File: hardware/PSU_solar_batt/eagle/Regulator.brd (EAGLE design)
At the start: 60.3 x 63.2 mm, 28 parts, among them IC1 MCP3550-60MS, IC2 MCP3550-60MS, IC3 MCP73831/OT

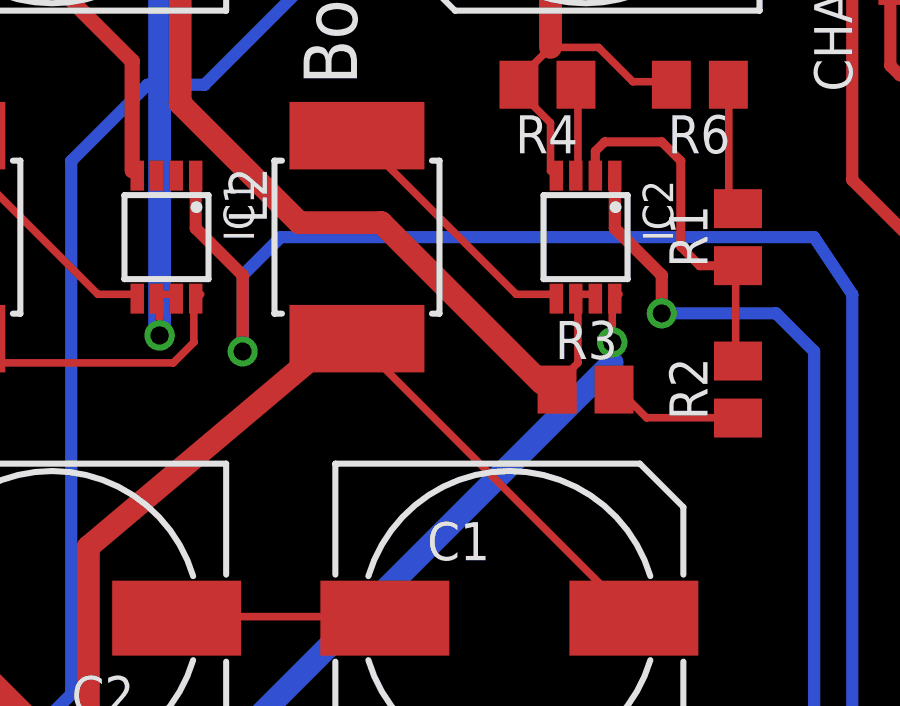
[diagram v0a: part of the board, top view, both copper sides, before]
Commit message: renames IC1 and IC2 to MCP1642 to avoid confusion (currently MCP3550 part is used instead because MCP1642 is not in the Microchip library)
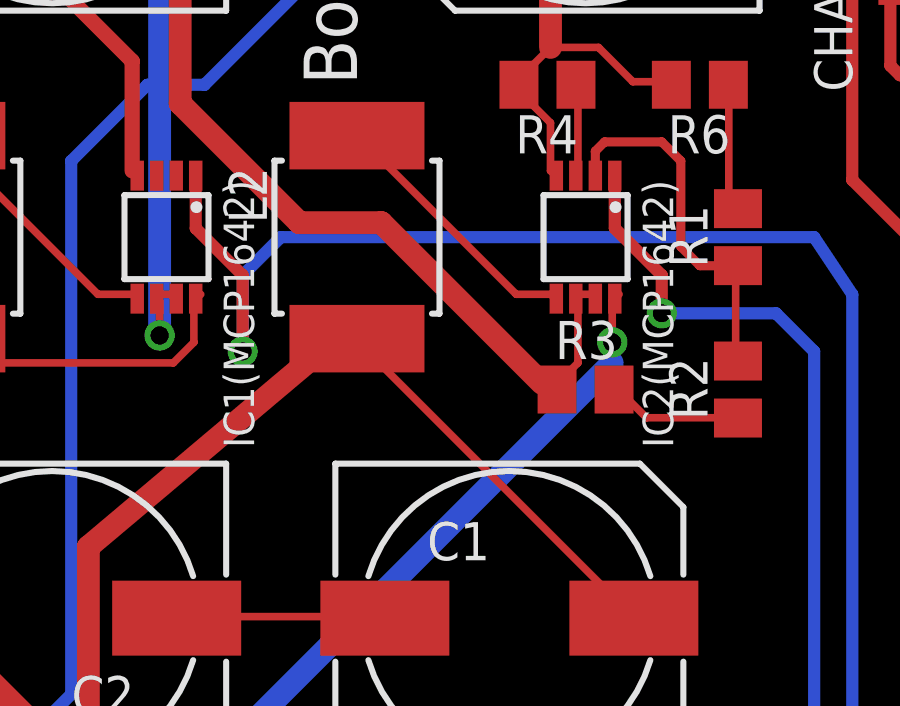
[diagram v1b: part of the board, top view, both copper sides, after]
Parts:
- renumbered IC1 to IC1(MCP1642), IC2 to IC2(MCP1642)
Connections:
- net N$1 renamed MCP1642
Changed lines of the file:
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@@
 <?xml version="1.0" encoding="utf-8"?>
 <!DOCTYPE eagle SYSTEM "eagle.dtd">
-<eagle version="7.2.0">
+<eagle version="7.1.0">
 <drawing>
 <settings>
@@
 <element name="C3" library="rcl" package="140CLH-1010" value="10uF" x="7.62" y="43.18" rot="R180"/>
 <element name="C4" library="rcl" package="140CLH-1010" value="10uF" x="25.4" y="43.18" rot="R180"/>
-<element name="IC1" library="microchip" package="MSOP8" value="MCP3550-60MS" x="11.43" y="30.48" smashed="yes" rot="R180">
+<element name="IC1(MCP1642)" library="microchip" package="MSOP8" value="MCP3550-60MS" x="11.43" y="30.48" smashed="yes" rot="R180">
 <attribute name="OC_NEWARK" value="69K0134" x="11.43" y="30.48" size="1.778" layer="27" rot="R180" display="off"/>
 <attribute name="MPN" value="MCP3550-60E/MS" x="11.43" y="30.48" size="1.778" layer="27" rot="R180" display="off"/>
@@
 <attribute name="NAME" x="13.335" y="32.385" size="1.016" layer="25" rot="R270"/>
 </element>
-<element name="IC2" library="microchip" package="MSOP8" value="MCP3550-60MS" x="25.4" y="30.48" smashed="yes" rot="R180">
+<element name="IC2(MCP1642)" library="microchip" package="MSOP8" value="MCP3550-60MS" x="25.4" y="30.48" smashed="yes" rot="R180">
 <attribute name="OC_NEWARK" value="69K0134" x="25.4" y="30.48" size="1.778" layer="27" rot="R180" display="off"/>
 <attribute name="MPN" value="MCP3550-60E/MS" x="25.4" y="30.48" size="1.778" layer="27" rot="R180" display="off"/>
@@
 </elements>
 <signals>
-<signal name="N$1">
+<signal name="MCP1642">
 <contactref element="C2" pad="+"/>
 <contactref element="L1" pad="2"/>
 <contactref element="REGULATORS" pad="4"/>
-<contactref element="IC1" pad="8"/>
+<contactref element="IC1(MCP1642)" pad="8"/>
 <wire x1="7.5438" y1="13.716" x2="7.5438" y2="10.287" width="0.762" layer="1"/>
 <wire x1="3.6576" y1="17.6022" x2="7.5438" y2="13.716" width="0.762" layer="1"/>
@@
 <contactref element="C1" pad="+"/>
 <contactref element="L2" pad="2"/>
-<contactref element="IC2" pad="8"/>
+<contactref element="IC2(MCP1642)" pad="8"/>
 <wire x1="17.8308" y1="26.9748" x2="26.9748" y2="17.8308" width="0.254" layer="1"/>
 <wire x1="26.9748" y1="17.8308" x2="27.01" y2="17.78" width="0.254" layer="1"/>
@@
 </signal>
 <signal name="3.3V">
-<contactref element="IC1" pad="4"/>
+<contactref element="IC1(MCP1642)" pad="4"/>
 <contactref element="C3" pad="+"/>
 <contactref element="3.3VOUT" pad="2"/>
@@
 <signal name="N$2">
 <contactref element="L1" pad="1"/>
-<contactref element="IC1" pad="5"/>
+<contactref element="IC1(MCP1642)" pad="5"/>
 <wire x1="9.144" y1="28.575" x2="10.287" y2="28.575" width="0.254" layer="1"/>
 <wire x1="3.8862" y1="33.8328" x2="9.144" y2="28.575" width="0.254" layer="1"/>
@@
 <signal name="N$4">
 <contactref element="L2" pad="1"/>
-<contactref element="IC2" pad="5"/>
+<contactref element="IC2(MCP1642)" pad="5"/>
 <wire x1="23.0886" y1="28.575" x2="24.2316" y2="28.575" width="0.254" layer="1"/>
 <wire x1="17.8308" y1="33.8328" x2="23.0886" y2="28.575" width="0.254" layer="1"/>
@@
 </signal>
 <signal name="5V">
-<contactref element="IC2" pad="4"/>
+<contactref element="IC2(MCP1642)" pad="4"/>
 <contactref element="R4" pad="2"/>
 <contactref element="C4" pad="+"/>
@@
 </signal>
 <signal name="N$10">
-<contactref element="IC2" pad="2"/>
+<contactref element="IC2(MCP1642)" pad="2"/>
 <contactref element="R2" pad="2"/>
 <contactref element="R1" pad="1"/>
@@
 </signal>
 <signal name="CONN">
-<contactref element="IC2" pad="3"/>
+<contactref element="IC2(MCP1642)" pad="3"/>
 <contactref element="R4" pad="1"/>
 <wire x1="25.146" y1="35.433" x2="25.146" y2="32.6898" width="0.254" layer="1"/>
@@
 </signal>
 <signal name="EN1">
-<contactref element="IC1" pad="1"/>
+<contactref element="IC1(MCP1642)" pad="1"/>
 <contactref element="SV1" pad="2"/>
 <wire x1="12.405" y1="32.53" x2="12.405" y2="30.775" width="0.4064" layer="1"/>
@@
 </signal>
 <signal name="EN2">
-<contactref element="IC2" pad="1"/>
+<contactref element="IC2(MCP1642)" pad="1"/>
 <contactref element="SV1" pad="1"/>
 <wire x1="26.375" y1="32.53" x2="26.375" y2="30.775" width="0.4064" layer="1"/>
@@
 <contactref element="3.3VOUT" pad="1"/>
 <contactref element="C2" pad="-"/>
-<contactref element="IC1" pad="7"/>
-<contactref element="IC1" pad="6"/>
+<contactref element="IC1(MCP1642)" pad="7"/>
+<contactref element="IC1(MCP1642)" pad="6"/>
 <contactref element="C4" pad="-"/>
 <contactref element="5VOUT1" pad="1"/>
 <contactref element="C1" pad="-"/>
-<contactref element="IC2" pad="7"/>
-<contactref element="IC2" pad="6"/>
+<contactref element="IC2(MCP1642)" pad="7"/>
+<contactref element="IC2(MCP1642)" pad="6"/>
 <contactref element="R3" pad="1"/>
 <wire x1="25.6032" y1="28.575" x2="25.146" y2="28.575" width="0.254" layer="1"/>
